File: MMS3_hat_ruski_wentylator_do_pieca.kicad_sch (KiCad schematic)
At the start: 12 parts, among them U4 AMS1117

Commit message: finished schematic
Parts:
- removed H7, H8, H9: (no value), PCM_JLCPCB:Hole_Tooling_JLCPCB, symbol PCM_JLCPCB-Manufacturing:Tooling Hole, PCM_JLCPCB, 1.152mm
- added J6: Conn_01x04_Socket, Connector_JST:JST_XH_S4B-XH-A_1x04_P2.50mm_Horizontal, symbol Connector:Conn_01x04_Socket
- added J9: Conn_01x06_Socket, Connector_JST:JST_XH_S6B-XH-A_1x06_P2.50mm_Horizontal, symbol Connector:Conn_01x06_Socket
- added Q1: AO3401A, Package_TO_SOT_SMD:SOT-23, symbol Transistor_FET:AO3401A
- added Q2: FMMT493, PCM_JLCPCB:Q_SOT-23, symbol PCM_JLCPCB-Transistors:NPN,FMMT493
- added R20: 2kΩ, PCM_JLCPCB:R_0603, symbol PCM_JLCPCB-Resistors:0603,2kΩ
- added R22: 0Ω, PCM_JLCPCB:R_0603, symbol PCM_JLCPCB-Resistors:0603,0Ω
- added R23: 15kΩ, PCM_JLCPCB:R_0402, symbol PCM_JLCPCB-Resistors:0402,15kΩ
- added R24: 10kΩ, PCM_JLCPCB:R_0402, symbol PCM_JLCPCB-Resistors:0402,10kΩ
- added R25: 1kΩ, PCM_JLCPCB:R_0603, symbol PCM_JLCPCB-Resistors:0603,1kΩ
- added R26: 10kΩ, PCM_JLCPCB:R_0603, symbol PCM_JLCPCB-Resistors:0603,10kΩ
- added R4: 36kΩ, PCM_JLCPCB:R_0603, symbol PCM_JLCPCB-Resistors:0603,36kΩ
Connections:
- net +3V3: now also J9.2 (Pin_2)
- net +5V: now also J6.2 (Pin_2)
- net GND: now also J6.1 (Pin_1), J9.1 (Pin_1), Q2.2 (E), R20.2, R23.2
- new net: Q2.1 (B), R26.2
- new net: Q1.1 (G), Q2.3 (C), R25.2
- new net Boost Converter/Boost_Out: Q1.2 (S), R22.2, R25.1
- new net CH32V003/PC4: R20.1, R4.2
- new net CN_MOT_VCC: J6.3 (Pin_3), Q1.3 (D), R22.1, R4.1
- new net CN_PWM: J6.4 (Pin_4), R24.1
- new net Hall_out: R23.1, R24.2
- new net PD3: J9.3 (Pin_3)
- new net PD4: J9.4 (Pin_4)
- new net PD5 (TX): J9.5 (Pin_5)
- new net PD6 (RX): J9.6 (Pin_6)
- new net PWM_Mosfet_gate: R26.1
- no-connect marks 2 -> 9
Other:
- added sheet Boost Converter (Boost_Converter.kicad_sch)
- added sheet CH32V003 (CH32V003.kicad_sch)
- sheet Power Connector ports: added VIN_BRD, VIN_Chainbus; removed none
- note added: "(GND)"
- note added: "(IC VCC)"
- note added: "Black"
- note added: "Blue"
- note added: "Brown"
- note added: "Fan Connector"
- note added: "Free MCU Pins"
- note added: "White/Yellow"
- note added: "max 3.158V"
- note added: "max 60V"
- title: MMS3 Hat template small (Change Me) -> MMS3_hat_ruski_wentylator_do_pieca

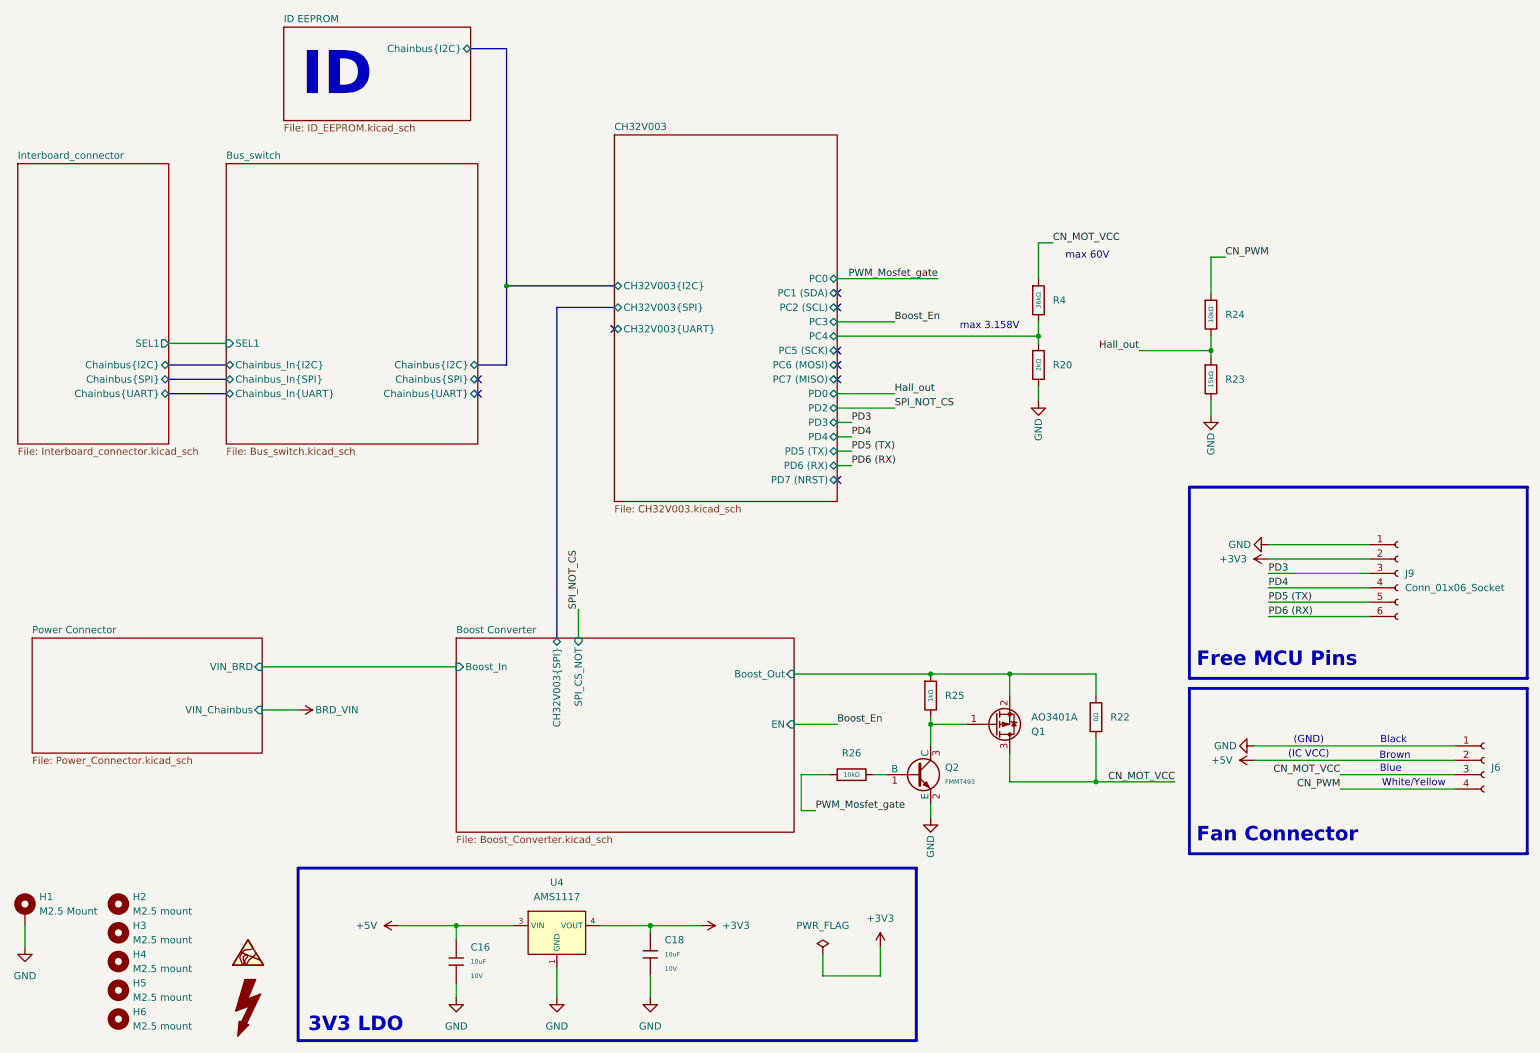
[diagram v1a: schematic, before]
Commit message: commit before removing all the diodes :"
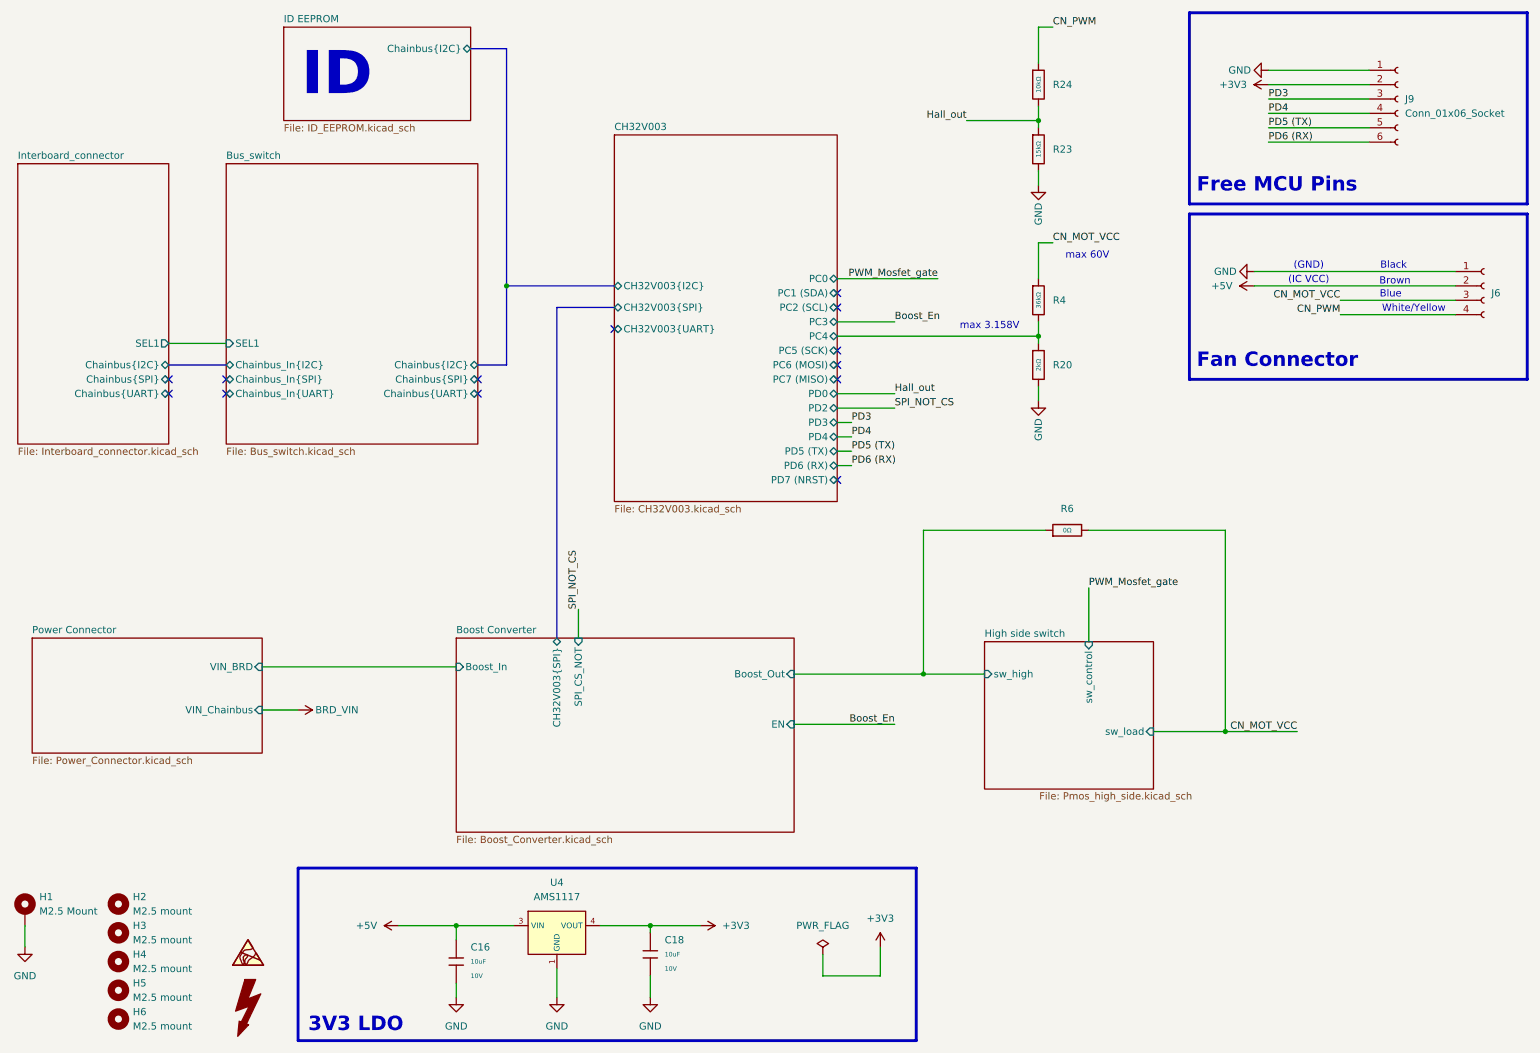
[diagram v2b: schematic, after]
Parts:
- removed Q1: AO3401A, Package_TO_SOT_SMD:SOT-23, symbol Transistor_FET:AO3401A
- removed Q2: FMMT493, PCM_JLCPCB:Q_SOT-23, symbol PCM_JLCPCB-Transistors:NPN,FMMT493
- removed R22: 0Ω, PCM_JLCPCB:R_0603, symbol PCM_JLCPCB-Resistors:0603,0Ω
- removed R25: 1kΩ, PCM_JLCPCB:R_0603, symbol PCM_JLCPCB-Resistors:0603,1kΩ
- removed R26: 10kΩ, PCM_JLCPCB:R_0603, symbol PCM_JLCPCB-Resistors:0603,10kΩ
- added R6: 0Ω, PCM_JLCPCB:R_0603, symbol PCM_JLCPCB-Resistors:0603,0Ω
- H1, H2, H3, H4, H5, H6: KiLib_Generator (none) -> mounting_hardware/mounting_hole
- J6, J9: KiLib_Generator (none) -> connector/JST
- R23, R24: Field4 (none) -> ${REFERENCE}
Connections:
- net Boost Converter/Boost_Out: now also R6.1
- net CN_MOT_VCC: now also R6.2
- no-connect marks 9 -> 13
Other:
- added sheet High side switch (Pmos_high_side.kicad_sch)
- moved on the sheet: J6, J9, R23, R24
